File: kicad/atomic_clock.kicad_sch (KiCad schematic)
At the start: 81 parts, among them J1 Conn_02x05_Top_Bottom, J10 Conn_02x05_Top_Bottom, J11 Conn_02x05_Top_Bottom, J12 USB_B_Micro 10118194-0001LF, J13 ARM_JTAG_SWD_10 3220-10-0100-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, J14 Conn_01x02_Male, J15 Conn_01x03_Female, J16 Conn_01x03_Male, J2 Conn_02x05_Top_Bottom, J3 Conn_02x05_Top_Bottom, J4 Conn_02x05_Top_Bottom, J5 USB_B_Micro 1051330001, J6 Conn_02x05_Top_Bottom, J7 Conn_02x05_Top_Bottom, J8 Conn_02x05_Top_Bottom, J9 Conn_02x05_Top_Bottom, Q1 Q_Dual_PMOS, Q2 Q_Dual_PMOS, SW1 SW_Push, SW2 SW_Push, U1 D198K, U10 ATSAMDA1E16B-A, U11 D198K, U12 D198K, U13 D198K, U14 D198K, U15 D198K, U16 MAX7221xWG, U17 D198K, U18 D198K, U19 D198K, U2 D198K, U20 NCP1117LPST33T3G, U21 mems_osc_st1630, U22 DHT20, U23 DCF77, U24 MCP73831-2-OT, U25 TXB0101, U3 D198K, U4 D198K, U5 MAX7221xWG, U6 D198K, U7 D198K, U8 D198K, U9 D198K

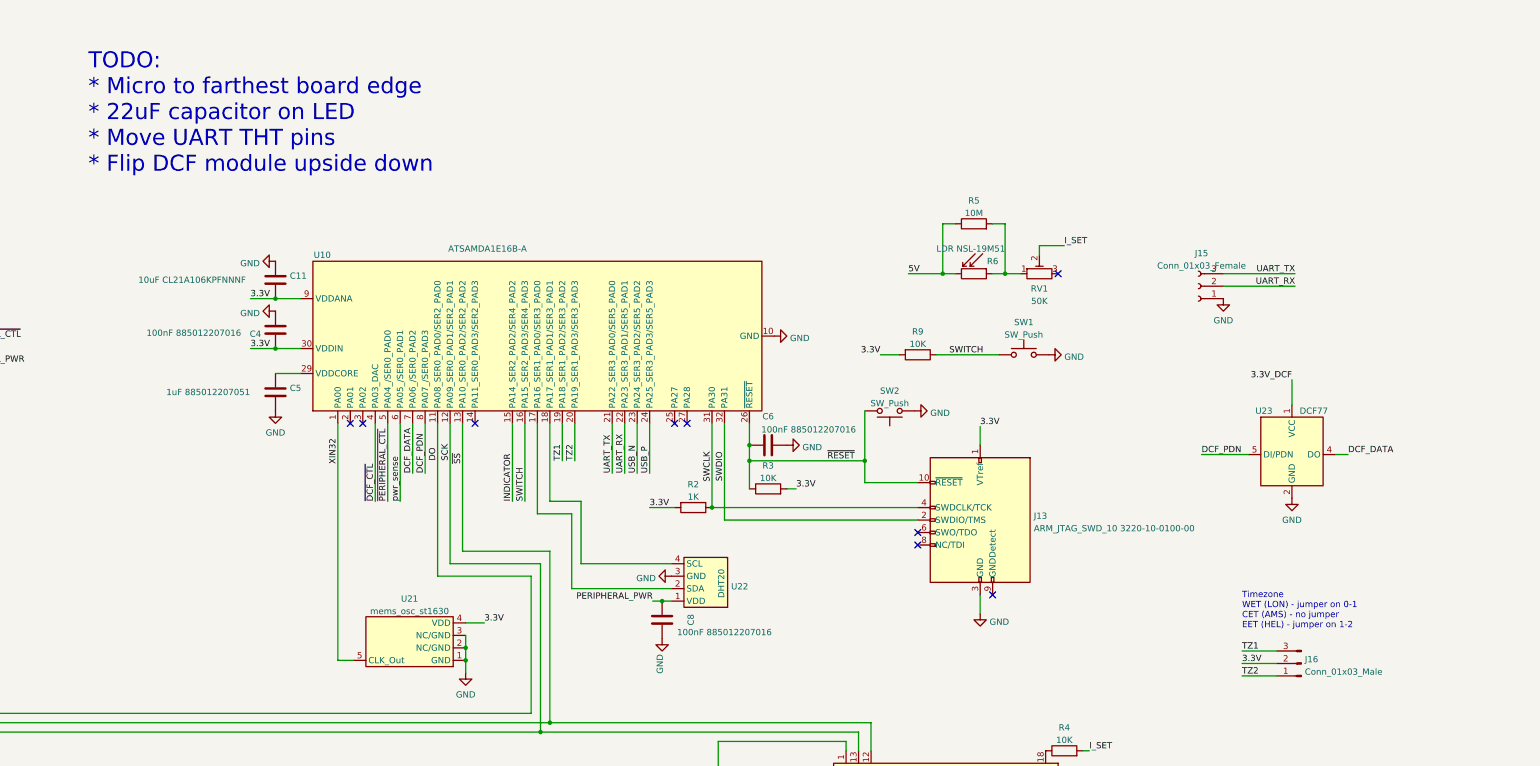
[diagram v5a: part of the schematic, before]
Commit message: Completed place and route of v2
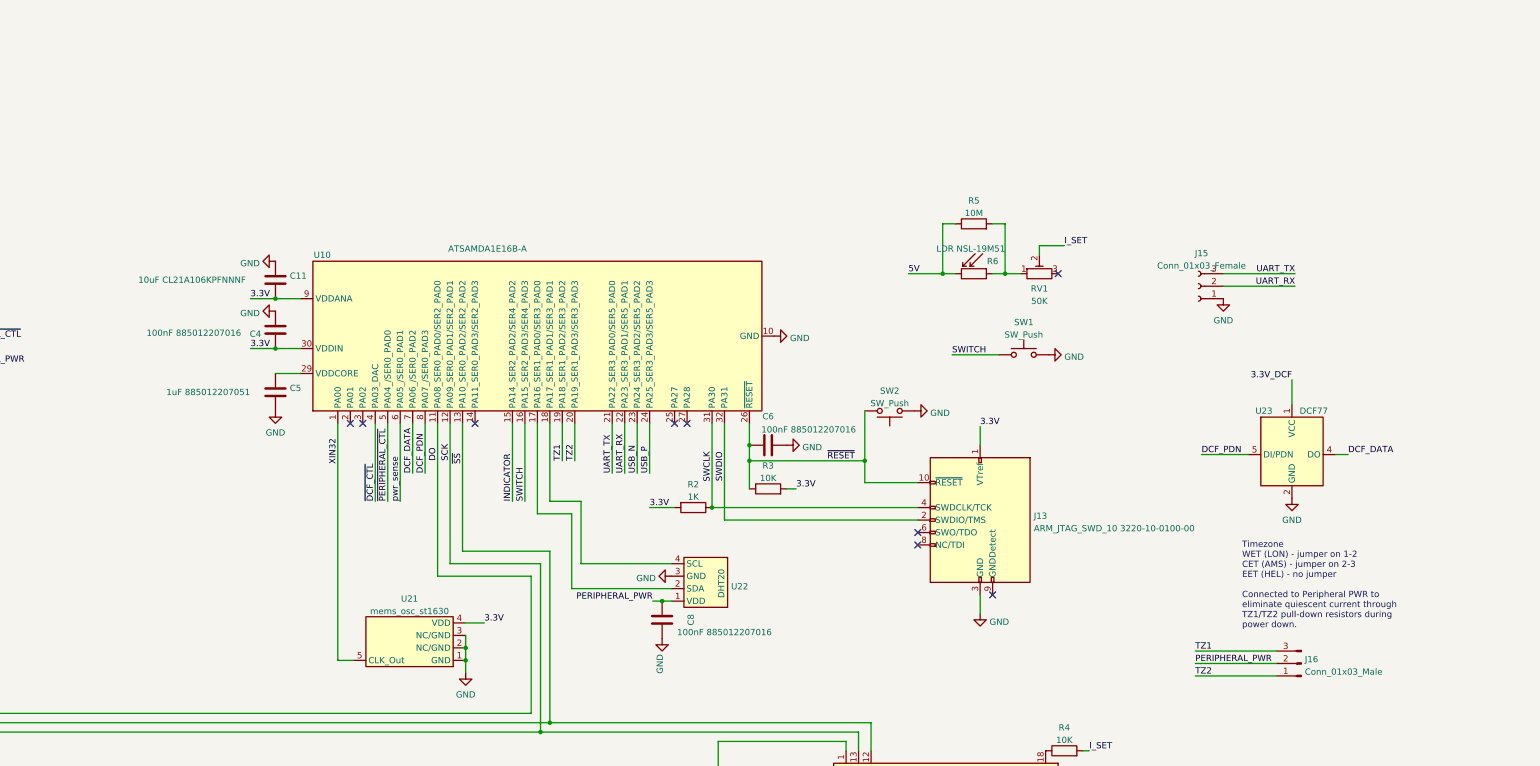
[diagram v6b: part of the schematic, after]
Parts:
- removed R9: 10K, Resistor_SMD:R_0805_2012Metric, symbol Device:R
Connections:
- net 3.3V: no longer J16.2 (Pin_2)
- net PERIPHERAL_PWR: now also J16.2 (Pin_2)
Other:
- note added: "Timezone WET (LON) - jumper on 1-2 CET (AMS) - jumper on 2-3 EET (HEL) - no jumper Connected to Peripheral PWR to eliminate quiescent current through TZ1/TZ2 pull-down resistors during power down."
- note removed: "TODO: * Micro to farthest board edge * 22uF capacitor on LED * Move UART THT pins * Flip DCF module upside down"
- note removed: "Timezone WET (LON) - jumper on 0-1 CET (AMS) - no jumper EET (HEL) - jumper on 1-2"
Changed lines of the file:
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@@
   (title_block
     (title "DCF-77 Radio controlled clock")
-    (date "2022-06-26")
-    (rev "v1.1")
+    (date "2022-10-28")
+    (rev "v2")
+    (comment 1 "Sources: https://github.com/erikvanzijst/radioclock")
     (comment 2 "License: MIT")
     (comment 3 "Email: erik.van.zijst@gmail.com")
@@
     (stroke (width 0) (type default) (color 0 0 0 0))
   )
-  (wire (pts (xy 457.835 167.64) (xy 464.82 167.64))
+  (wire (pts (xy 448.31 167.64) (xy 464.82 167.64))
     (stroke (width 0) (type default) (color 0 0 0 0))
   )
@@
     (stroke (width 0) (type default) (color 0 0 0 0))
   )
-  (wire (pts (xy 387.985 107.315) (xy 384.175 107.315))
-    (stroke (width 0) (type default) (color 0 0 0 0))
-  )
   (wire (pts (xy 146.05 312.42) (xy 146.05 314.96))
     (stroke (width 0) (type default) (color 0 0 0 0))
@@
     (stroke (width 0) (type default) (color 0 0 0 0))
   )
-  (wire (pts (xy 457.835 172.72) (xy 464.82 172.72))
+  (wire (pts (xy 448.31 172.72) (xy 464.82 172.72))
     (stroke (width 0) (type default) (color 0 0 0 0))
   )
@@
     (stroke (width 0) (type default) (color 0 0 0 0))
   )
-  (wire (pts (xy 395.605 107.315) (xy 408.305 107.315))
+  (wire (pts (xy 398.78 107.315) (xy 408.305 107.315))
     (stroke (width 0) (type default) (color 0 0 0 0))
   )
@@
     (stroke (width 0) (type default) (color 0 0 0 0))
   )
-  (wire (pts (xy 457.835 170.18) (xy 464.82 170.18))
+  (wire (pts (xy 448.31 170.18) (xy 464.82 170.18))
     (stroke (width 0) (type default) (color 0 0 0 0))
   )
@@
     (effects (font (size 1.27 1.27)) (justify left bottom))
   )
-  (text "TODO:\n* Micro to farthest board edge\n* 22uF capacitor on LED\n* Move UART THT pins\n* Flip DCF module upside down"
-    (at 222.885 70.485 0)
-    (effects (font (size 3.27 3.27)) (justify left bottom))
-  )
-  (text "Timezone\nWET (LON) - jumper on 0-1\nCET (AMS) - no jumper\nEET (HEL) - jumper on 1-2"
+  (text "Timezone\nWET (LON) - jumper on 1-2\nCET (AMS) - jumper on 2-3\nEET (HEL) - no jumper\n\nConnected to Peripheral PWR to\neliminate quiescent current through\nTZ1/TZ2 pull-down resistors during\npower down."
     (at 457.835 163.195 0)
     (effects (font (size 1.27 1.27)) (justify left bottom))
@@
     (effects (font (size 1.27 1.27)) (justify left bottom))
   )
-  (label "3.3V" (at 384.175 107.315 180)
-    (effects (font (size 1.27 1.27)) (justify right bottom))
-  )
   (label "USB_N" (at 334.645 131.445 90)
     (effects (font (size 1.27 1.27)) (justify left bottom))
@@
     (effects (font (size 1.27 1.27)) (justify left bottom))
   )
-  (label "TZ2" (at 457.835 172.72 0)
+  (label "TZ2" (at 448.31 172.72 0)
     (effects (font (size 1.27 1.27)) (justify left bottom))
   )
@@
     (effects (font (size 1.27 1.27)) (justify left bottom))
   )
-  (label "SWITCH" (at 405.13 107.315 180)
-    (effects (font (size 1.27 1.27)) (justify right bottom))
+  (label "SWITCH" (at 398.78 107.315 0)
+    (effects (font (size 1.27 1.27)) (justify left bottom))
   )
   (label "1DP2" (at 378.46 241.3 180)
@@
     (effects (font (size 1.27 1.27)) (justify left bottom))
   )
-  (label "3.3V" (at 457.835 170.18 0)
+  (label "PERIPHERAL_PWR" (at 448.31 170.18 0)
     (effects (font (size 1.27 1.27)) (justify left bottom))
   )
@@
     (effects (font (size 1.27 1.27)) (justify left bottom))
   )
-  (label "TZ1" (at 457.835 167.64 0)
+  (label "TZ1" (at 448.31 167.64 0)
     (effects (font (size 1.27 1.27)) (justify left bottom))
   )
@@
     (pin "9")
   )
-  (symbol (lib_id "Device:R") (at 391.795 107.315 270) (unit 1)
-    (in_bom yes) (on_board yes) (fields_autoplaced)
-    (property "Reference" "R9" (id 0) (at 391.795 102.5992 90))
-    (property "Value" "10K" (id 1) (at 391.795 105.1361 90))
-    (property "Footprint" "Resistor_SMD:R_0805_2012Metric" (id 2) (at 391.795 105.537 90)
-      (effects (font (size 1.27 1.27)) hide)
-    )
-    (property "Datasheet" "https://www.mouser.be/datasheet/2/219/RK73H-1825326.pdf" (id 3) (at 391.795 107.315 0)
-      (effects (font (size 1.27 1.27)) hide)
-    )
-    (property "Price" "0.017" (id 4) (at 391.795 107.315 0)
-      (effects (font (size 1.27 1.27)) hide)
-    )
-    (pin "1")
-    (pin "2")
-  )
   (symbol (lib_id "local_symbols:mems_osc_st1630") (at 288.29 165.735 180) (unit 1)
     (in_bom yes) (on_board yes) (fields_autoplaced)
@@
       (reference "R8") (unit 1) (value "470R") (footprint "Resistor_SMD:R_0805_2012Metric")
     )
-    (path "/a9908e0d-28fc-483c-b37b-502805421341"
-      (reference "R9") (unit 1) (value "10K") (footprint "Resistor_SMD:R_0805_2012Metric")
-    )
     (path "/9a001c4e-10bc-4c38-af7c-0bbd97b8b2a5"

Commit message: Add schematic pdf
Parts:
- J16: footprint (none) -> Connector_PinHeader_2.54mm:PinHeader_1x03_P2.54mm_Vertical
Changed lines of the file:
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@@
       (effects (font (size 1.27 1.27)) (justify right))
     )
-    (property "Footprint" "" (id 2) (at 469.9 170.18 0)
+    (property "Footprint" "Connector_PinHeader_2.54mm:PinHeader_1x03_P2.54mm_Vertical" (id 2) (at 469.9 170.18 0)
       (effects (font (size 1.27 1.27)) hide)
     )

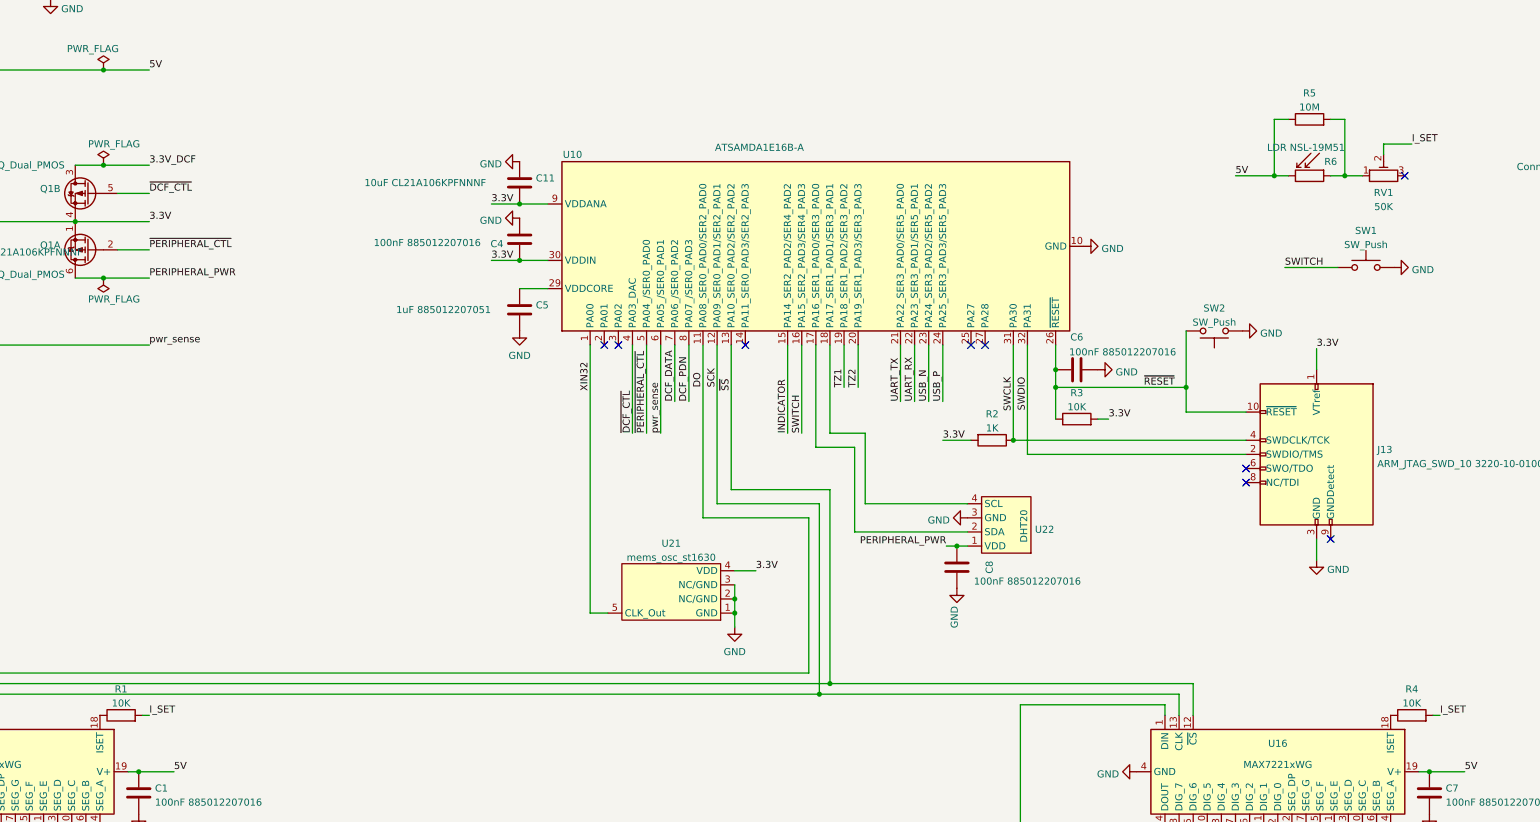
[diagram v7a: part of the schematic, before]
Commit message: Tune analog brightness control circuitry
Real world testing showed the 10K resistor on each driver chip to
be unnecessary and the 10MOhm parallel to the LDR to be overkill.
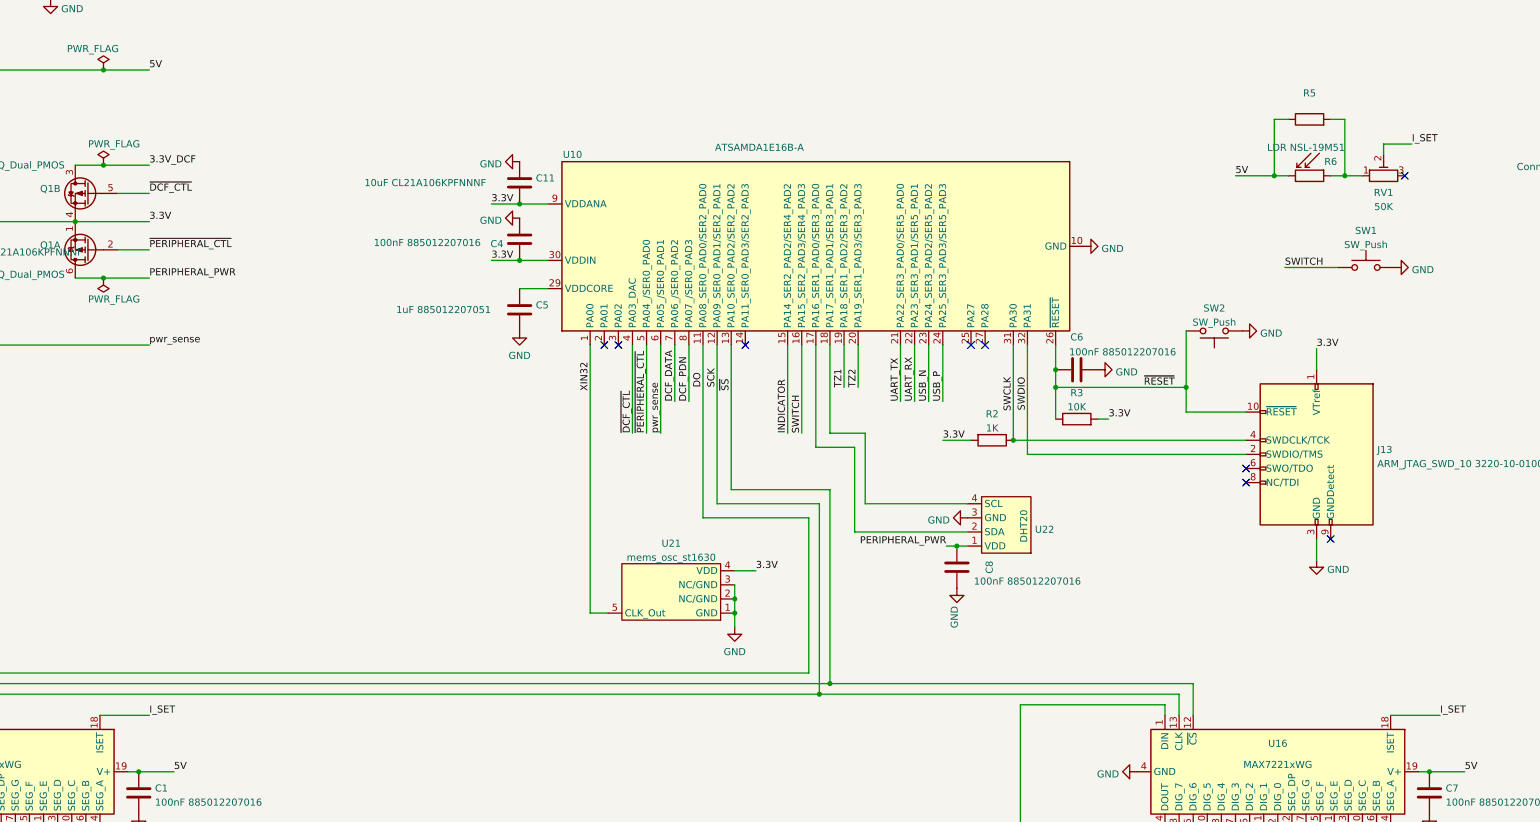
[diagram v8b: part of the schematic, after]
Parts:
- removed R1, R4: 10K, Resistor_SMD:R_0805_2012Metric, symbol Device:R
- R5: value 10M -> (none)
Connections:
- net I_SET: now also U16.18 (ISET), U5.18 (ISET)
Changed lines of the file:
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@@
     (stroke (width 0) (type default) (color 0 0 0 0))
   )
-  (wire (pts (xy 425.45 187.96) (xy 426.72 187.96))
+  (wire (pts (xy 417.83 187.96) (xy 426.72 187.96))
     (stroke (width 0) (type default) (color 0 0 0 0))
   )
@@
     (stroke (width 0) (type default) (color 0 0 0 0))
   )
-  (wire (pts (xy 193.04 187.96) (xy 194.31 187.96))
+  (wire (pts (xy 185.42 187.96) (xy 194.31 187.96))
     (stroke (width 0) (type default) (color 0 0 0 0))
   )
@@
     (in_bom yes) (on_board yes) (fields_autoplaced)
     (property "Reference" "R5" (id 0) (at 403.225 75.9292 90))
-    (property "Value" "10M" (id 1) (at 403.225 78.4661 90))
+    (property "Value" "" (id 1) (at 403.225 78.4661 90))
     (property "Footprint" "Resistor_SMD:R_0805_2012Metric" (id 2) (at 403.225 82.423 90)
       (effects (font (size 1.27 1.27)) hide)
@@
     (pin "1")
   )
-  (symbol (lib_id "Device:R") (at 421.64 187.96 90) (unit 1)
-    (in_bom yes) (on_board yes) (fields_autoplaced)
-    (property "Reference" "R4" (id 0) (at 421.64 183.2442 90))
-    (property "Value" "10K" (id 1) (at 421.64 185.7811 90))
-    (property "Footprint" "Resistor_SMD:R_0805_2012Metric" (id 2) (at 421.64 189.738 90)
-      (effects (font (size 1.27 1.27)) hide)
-    )
-    (property "Datasheet" "https://www.mouser.be/datasheet/2/219/RK73H-1825326.pdf" (id 3) (at 421.64 187.96 0)
-      (effects (font (size 1.27 1.27)) hide)
-    )
-    (property "Price" "0.017" (id 4) (at 421.64 187.96 0)
-      (effects (font (size 1.27 1.27)) hide)
-    )
-    (pin "1")
-    (pin "2")
-  )
   (symbol (lib_id "Device:R") (at 102.87 55.245 90) (mirror x) (unit 1)
     (in_bom yes) (on_board yes)
@@
     (pin "9")
   )
-  (symbol (lib_id "Device:R") (at 189.23 187.96 90) (unit 1)
-    (in_bom yes) (on_board yes) (fields_autoplaced)
-    (property "Reference" "R1" (id 0) (at 189.23 183.2442 90))
-    (property "Value" "10K" (id 1) (at 189.23 185.7811 90))
-    (property "Footprint" "Resistor_SMD:R_0805_2012Metric" (id 2) (at 189.23 189.738 90)
-      (effects (font (size 1.27 1.27)) hide)
-    )
-    (property "Datasheet" "https://www.mouser.be/datasheet/2/219/RK73H-1825326.pdf" (id 3) (at 189.23 187.96 0)
-      (effects (font (size 1.27 1.27)) hide)
-    )
-    (property "Price" "0.017" (id 4) (at 189.23 187.96 0)
-      (effects (font (size 1.27 1.27)) hide)
-    )
-    (pin "1")
-    (pin "2")
-  )
   (symbol (lib_id "Display_Character:D198K") (at 443.23 304.8 0) (unit 1)
     (in_bom yes) (on_board yes) (fields_autoplaced)
@@
       (reference "Q2") (unit 2) (value "Q_Dual_PMOS") (footprint "Package_TO_SOT_SMD:SOT-363_SC-70-6")
     )
-    (path "/f232cb03-7a25-4f72-8978-0fb0c44c6472"
-      (reference "R1") (unit 1) (value "10K") (footprint "Resistor_SMD:R_0805_2012Metric")
-    )
     (path "/535c868d-57d5-4fad-a0bd-284557e42489"
       (reference "R2") (unit 1) (value "1K") (footprint "Resistor_SMD:R_0805_2012Metric")
@@
       (reference "R3") (unit 1) (value "10K") (footprint "Resistor_SMD:R_0805_2012Metric")
     )
-    (path "/e0f63686-b391-456e-b177-37c9b0bcf36f"
-      (reference "R4") (unit 1) (value "10K") (footprint "Resistor_SMD:R_0805_2012Metric")
-    )
     (path "/775007b4-9977-44d0-b442-6b19bea3e6ed"
-      (reference "R5") (unit 1) (value "10M") (footprint "Resistor_SMD:R_0805_2012Metric")
+      (reference "R5") (unit 1) (value "1M") (footprint "Resistor_SMD:R_0805_2012Metric")
     )
     (path "/d6f413db-b042-43f9-83a2-89f146cd5a00"
